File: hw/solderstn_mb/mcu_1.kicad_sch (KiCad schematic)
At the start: 23 parts, among them Q2001 DMG1012T, SW2001 Pushbutton_SMD_TS-1102W-4316, SW2002 Pushbutton_SMD_TS-1102W-4316, U2001 MCP1316T-26LE-OT, U2002 W25Q64FV, U401 STM32F429VITx, Y2001 TSX-3225 16.0000MF18X-AC3

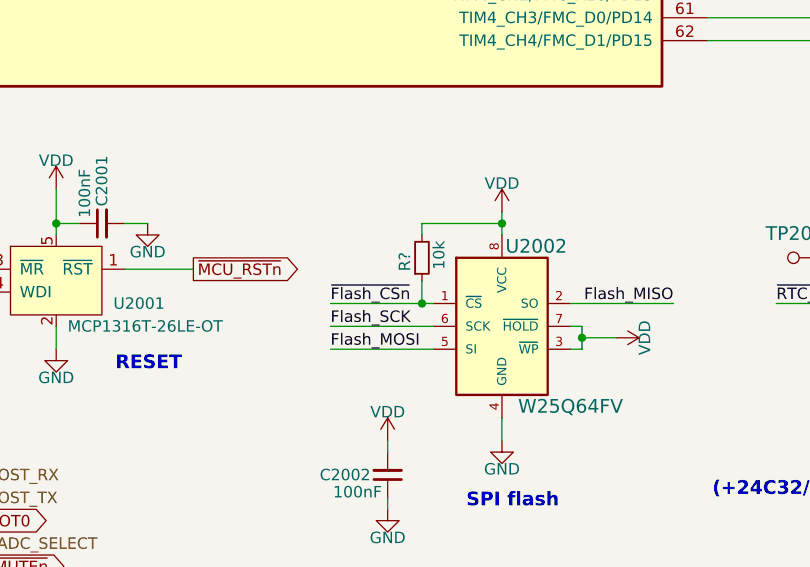
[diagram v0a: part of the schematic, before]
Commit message: Placeholder 3d-models for rear-panel (w. conns), PSU, Bottom-plate, front-panel (w. conns), outer fp
With these placeholder mech. objects, the build-in 3d view of MB pcb features most of the mechanical
objects that constrain components placements. So 3d-view can be used to quickly check and iterate
placements to avoid 3d collisions, without having to first export MB STEP into FreeCAD and muck around
only to have to repeat again for each iteration
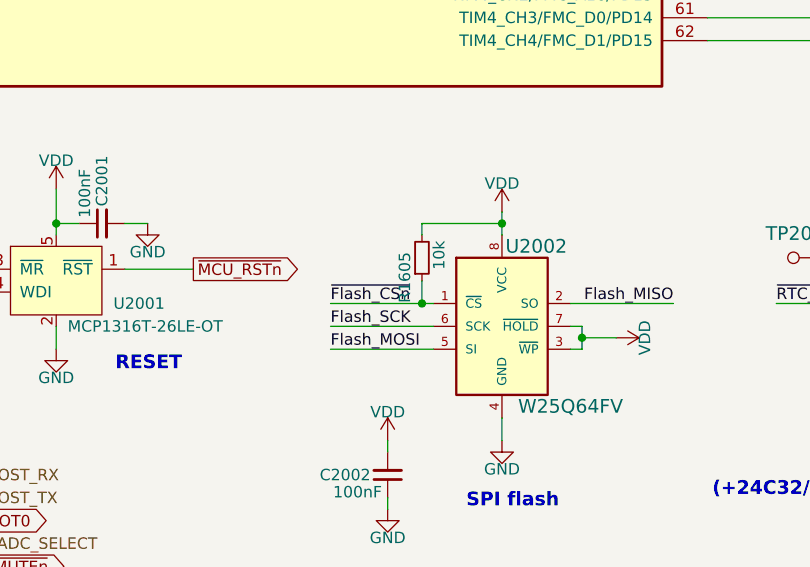
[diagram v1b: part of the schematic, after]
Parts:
- gave numbers to parts that had none: 1
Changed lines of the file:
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@@
   (symbol (lib_id "Device:R_Small") (at 213.36 130.81 0) (mirror x) (unit 1)
     (in_bom yes) (on_board yes)
-    (property "Reference" "R?" (id 0) (at 211.455 130.175 90)
+    (property "Reference" "R1605" (id 0) (at 211.455 130.175 90)
       (effects (font (size 1.27 1.27)) (justify left))
     )
